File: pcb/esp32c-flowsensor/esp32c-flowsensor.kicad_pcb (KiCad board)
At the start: 2 copper layers, 85.1 x 40 mm, 30 parts, among them J1 NTC1, J2 NTC2, J3 Heater, J4 ALARM, J5 12V In, Q1 BC817, Q2 IRF540N, Q3 BC817, U1 AMS1117-5.0, U2 esp32-c3-ebay

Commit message: Pcb update
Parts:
- added D4: LED, LED_SMD:LED_0805_2012Metric_Pad1.15x1.40mm_HandSolder, F.Cu at (98.5, 69.8)
- added D5: LED, LED_SMD:LED_0805_2012Metric_Pad1.15x1.40mm_HandSolder, F.Cu at (98.5, 72.9)
- added D6: LED, LED_SMD:LED_0805_2012Metric_Pad1.15x1.40mm_HandSolder, F.Cu at (98.5, 75.9)
- added R10: 10K, Resistor_SMD:R_0805_2012Metric_Pad1.20x1.40mm_HandSolder, F.Cu at (103.2, 72.7)
- added R11: 10K, Resistor_SMD:R_0805_2012Metric_Pad1.20x1.40mm_HandSolder, F.Cu at (103.2, 75.7)
- added R9: 10K, Resistor_SMD:R_0805_2012Metric_Pad1.20x1.40mm_HandSolder, F.Cu at (103.2, 69.8)
- Q2: footprint Package_TO_SOT_THT:TO-220-3_Vertical -> Package_TO_SOT_THT:TO-220-3_Horizontal_TabDown
- moved R3 10.6 mm to (96.3, 88.4)
- moved Q1 10.6 mm to (99.0, 83.8)
- moved R4 9.88 mm to (94.5, 83.8), turned to 180 degrees
- moved Q2 9.20 mm to (86.7, 81.3), turned to 0 degrees
- moved F2 6.75 mm to (67.6, 80.0)
- moved R7 6.42 mm to (103.2, 84.0), turned to -90 degrees
- moved D1 6.24 mm to (78.0, 73.3)
- moved J3 6.24 mm to (75.8, 65.9)
- moved J5 6.24 mm to (65.5, 65.9)
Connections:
- U2 pad 1: unconnected-(U2-gpio5-Pad1) -> STILL_LED
- U2 pad 2: unconnected-(U2-gop6-Pad2) -> AIR_LED
- U2 pad 3: unconnected-(U2-gpio7-Pad3) -> FLOW_LED
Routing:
- net GND: track 317.8 -> 290.2 mm
- net HEATER_POWER: track 19.8 -> 35.1 mm
- net 5V: track 98.5 -> 107.8 mm
- net 12V_SENSE: track 50.6 -> 59.1 mm
- net HEATER_PWM: track 12.0 -> 4.60 mm
- net 12IN: track 27.4 -> 21.8 mm
- net Net-(Q2-G): track 3.26 -> 8.60 mm
- net STILL_LED: track 0.00 -> 3.79 mm
- net FLOW_LED: track 0.00 -> 3.65 mm
- net AIR_LED: track 0.00 -> 3.62 mm
- net Net-(D6-A): track 0.00 -> 2.81 mm
- net Net-(D5-A): track 0.00 -> 2.78 mm
- net Net-(D4-A): track 0.00 -> 2.74 mm
- net 12VF: track 99.0 -> 96.6 mm
- net Net-(Q1-B): track 4.77 -> 3.38 mm
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- added copper zone on B.Cu, net HEATER_POWER
- added copper zone on F.Cu, net HEATER_POWER

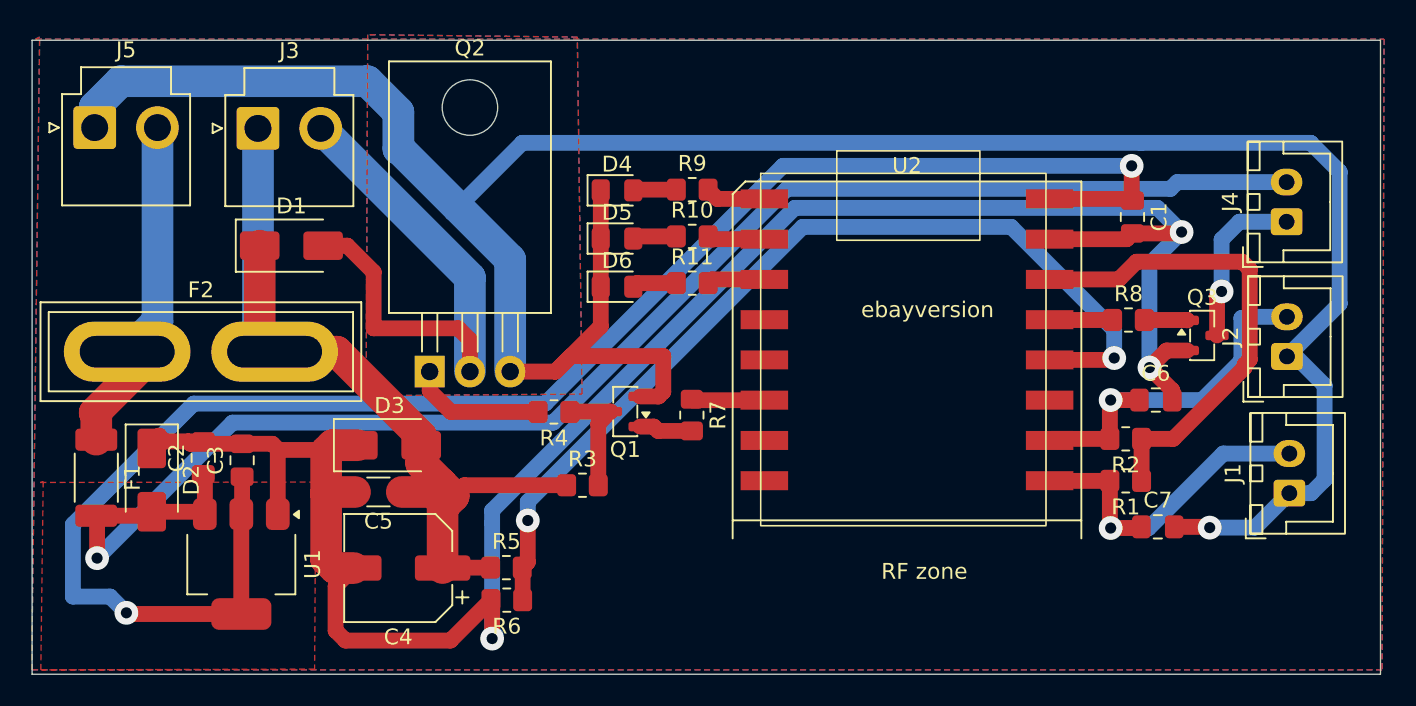
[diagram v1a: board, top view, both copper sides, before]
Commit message: Stopping work in favour of exhaust elbow sensing
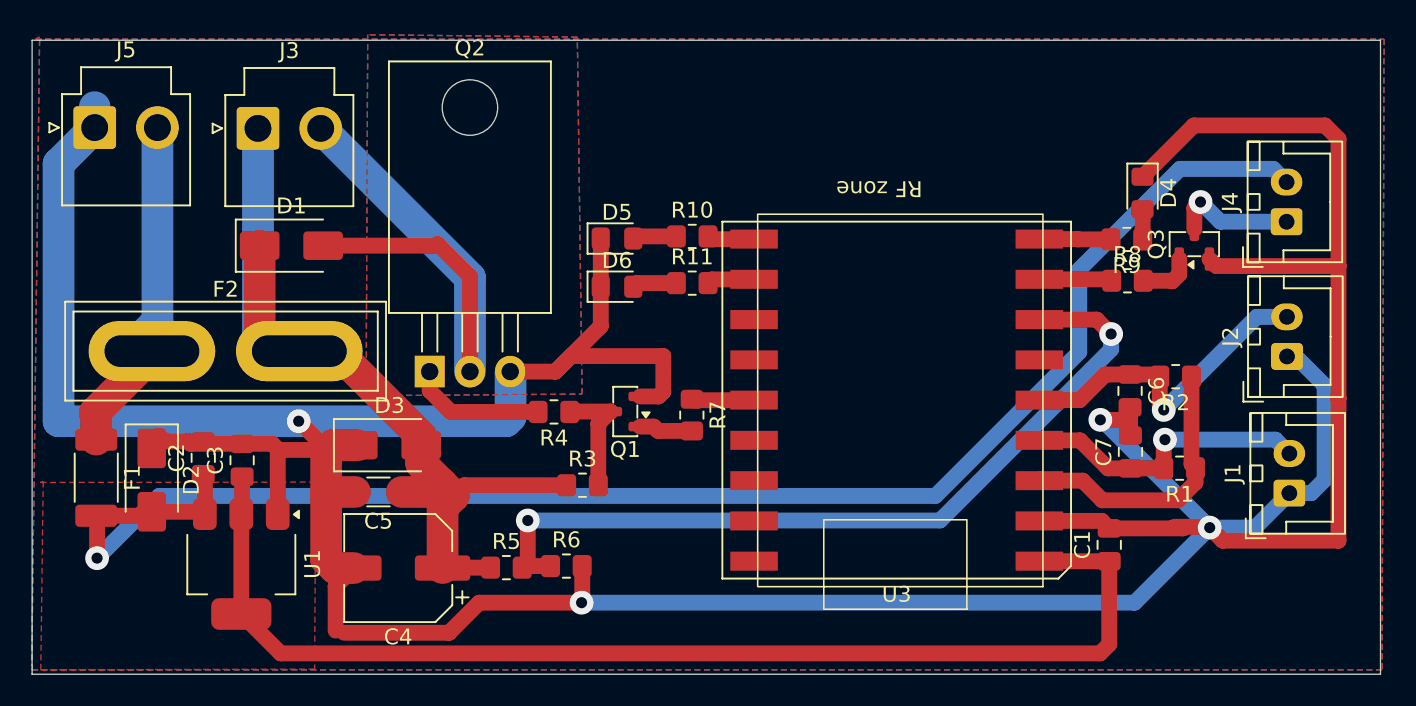
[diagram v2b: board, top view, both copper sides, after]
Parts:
- removed U2: esp32-c3-ebay, Library:ESP-C3-Zero-ebay
- added U3: ESP32-C3-Waveshare, iebSpecials:ESP-C3-Zero-Waveshare, F.Cu at (125.4, 93.3)
- moved D4 33.2 mm to (131.7, 70.0), turned to -90 degrees
- moved R9 27.6 mm to (130.7, 72.9), turned to 180 degrees
- moved C1 20.7 mm to (129.6, 92.2), turned to 90 degrees
- moved Q3 5.78 mm to (134.9, 73.2), turned to 90 degrees
- moved R2 5.03 mm to (133.8, 81.6)
- moved C7 5.03 mm to (130.9, 86.3), turned to 90 degrees
- moved R6 4.33 mm to (95.3, 93.5), turned to 0 degrees
- moved R1 3.49 mm to (134.0, 87.3)
- moved R8 2.48 mm to (130.7, 75.5)
- moved C6 1.72 mm to (130.9, 82.5), turned to -90 degrees
- moved F2 1.56 mm to (69.2, 80.0)
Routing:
- net 5V: track 107.8 -> 74.3 mm, vias 2 -> 0
- net 3V3: track 30.6 -> 17.8 mm
- net 12V_SENSE: track 59.1 -> 52.1 mm
- net GND: track 290.2 -> 285.1 mm
- net 12VF: track 96.6 -> 100.3 mm
- net NTC1: track 21.9 -> 18.6 mm
- net Net-(J4-Pin_1): track 10.7 -> 7.83 mm
- net NTC2: track 22.9 -> 20.7 mm
- net Net-(D4-A): track 2.74 -> 1.91 mm
- net STILL_LED: track 3.79 -> 4.53 mm
- net Net-(Q3-B): track 2.72 -> 3.42 mm
- net ALARM_SOUND: track 3.96 -> 4.60 mm
